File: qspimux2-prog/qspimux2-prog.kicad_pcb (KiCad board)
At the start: 4 copper layers, 58 x 38 mm, 94 parts, among them J101 Conn_02x03_Odd_Even, J201 Conn_01x10_MountingPin, J301 Conn_01x03_MountingPin, J401 Conn_01x08_MountingPin, J501 Conn_01x08_MountingPin, J701 USB_B_Micro, J901 Conn_01x03_MountingPin, Q601 BSS138, Q901 FDG6335N, U101 STM32F042C6Tx, U201 SN74LVC1T45DCK, U202 SN74LVC1T45DCK, U203 SN74LVC1T45DCK, U204 SN74LVC1T45DCK, U205 SN74LVC1T45DCK, U206 SN74LVC1T45DCK, U207 SN74LVC1T45DCK, U301 SN74LVC1T45DCK, U302 SN74LVC1T45DCK, U401 TLP176AM, U402 TLP176AM, U403 TLP176AM, U404 TLP176AM, U501 TLP290-4, U601 MIC5504-3.3YM5, U602 AP2127K-ADJ, U701 NUP2202

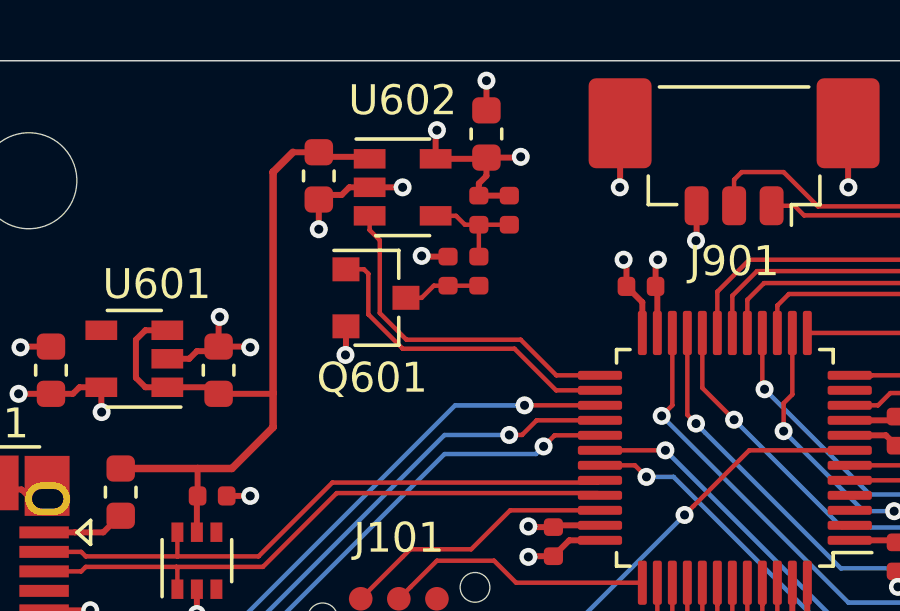
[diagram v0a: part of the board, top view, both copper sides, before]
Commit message: qspimux2-prog: add pull down resistors to enable and select inputs of vdd regulator
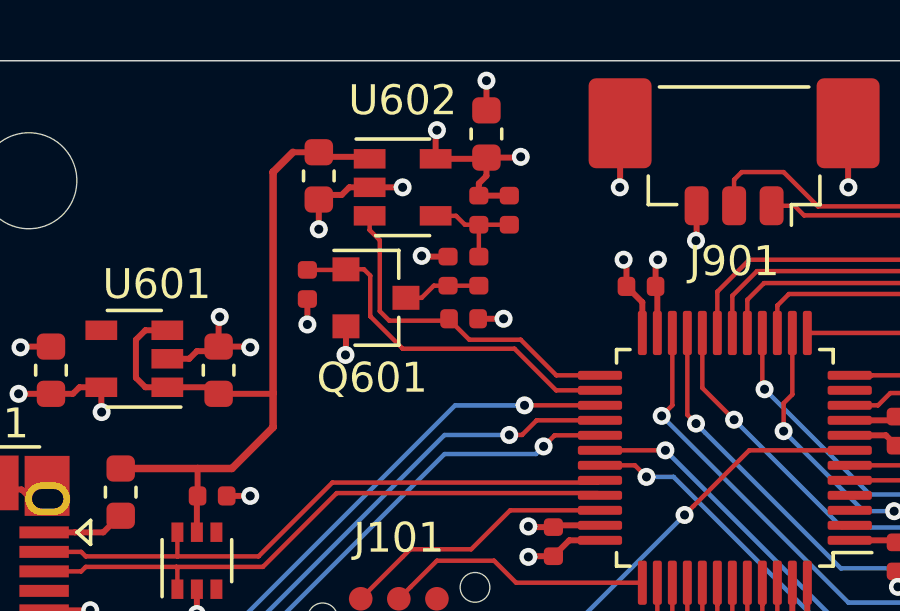
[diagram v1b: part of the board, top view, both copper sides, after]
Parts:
- added R601: 10k, Resistor_SMD:R_0402_1005Metric, F.Cu at (118.5, 105.6)
- added R602: 10k, Resistor_SMD:R_0402_1005Metric, F.Cu at (113.3, 104.5)
- renumbered R601 to R603, R602 to R604, R603 to R605
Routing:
- net GND: track 105.5 -> 107.2 mm, vias 62 -> 64
- net /VDD_SEL: track 10.9 -> 12.2 mm
